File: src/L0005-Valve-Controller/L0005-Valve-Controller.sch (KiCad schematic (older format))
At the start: 25 parts, among them J1 Jumper_NO, J2 Jumper_NO, P1 3220-20-0200-00, P2 140-504-415-000, U1 LPC54113J256BD64QL, U2 LMS8117AMP-3.3_NOPB

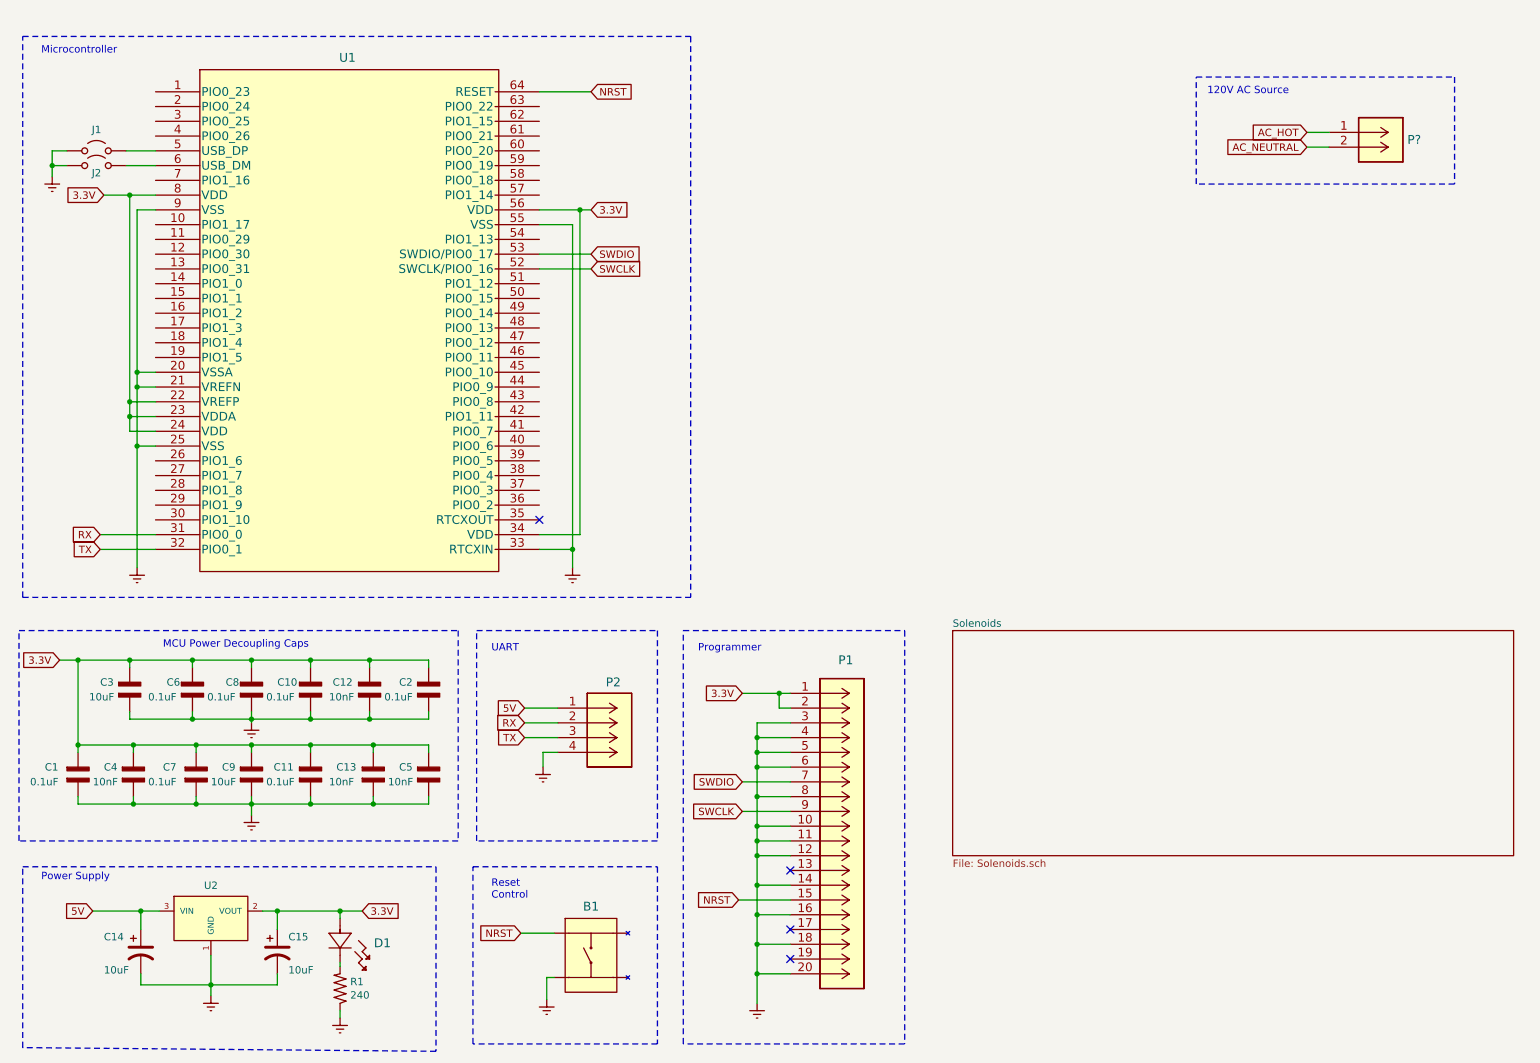
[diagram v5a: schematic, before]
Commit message: Added servo-actuated ball valves to schematic
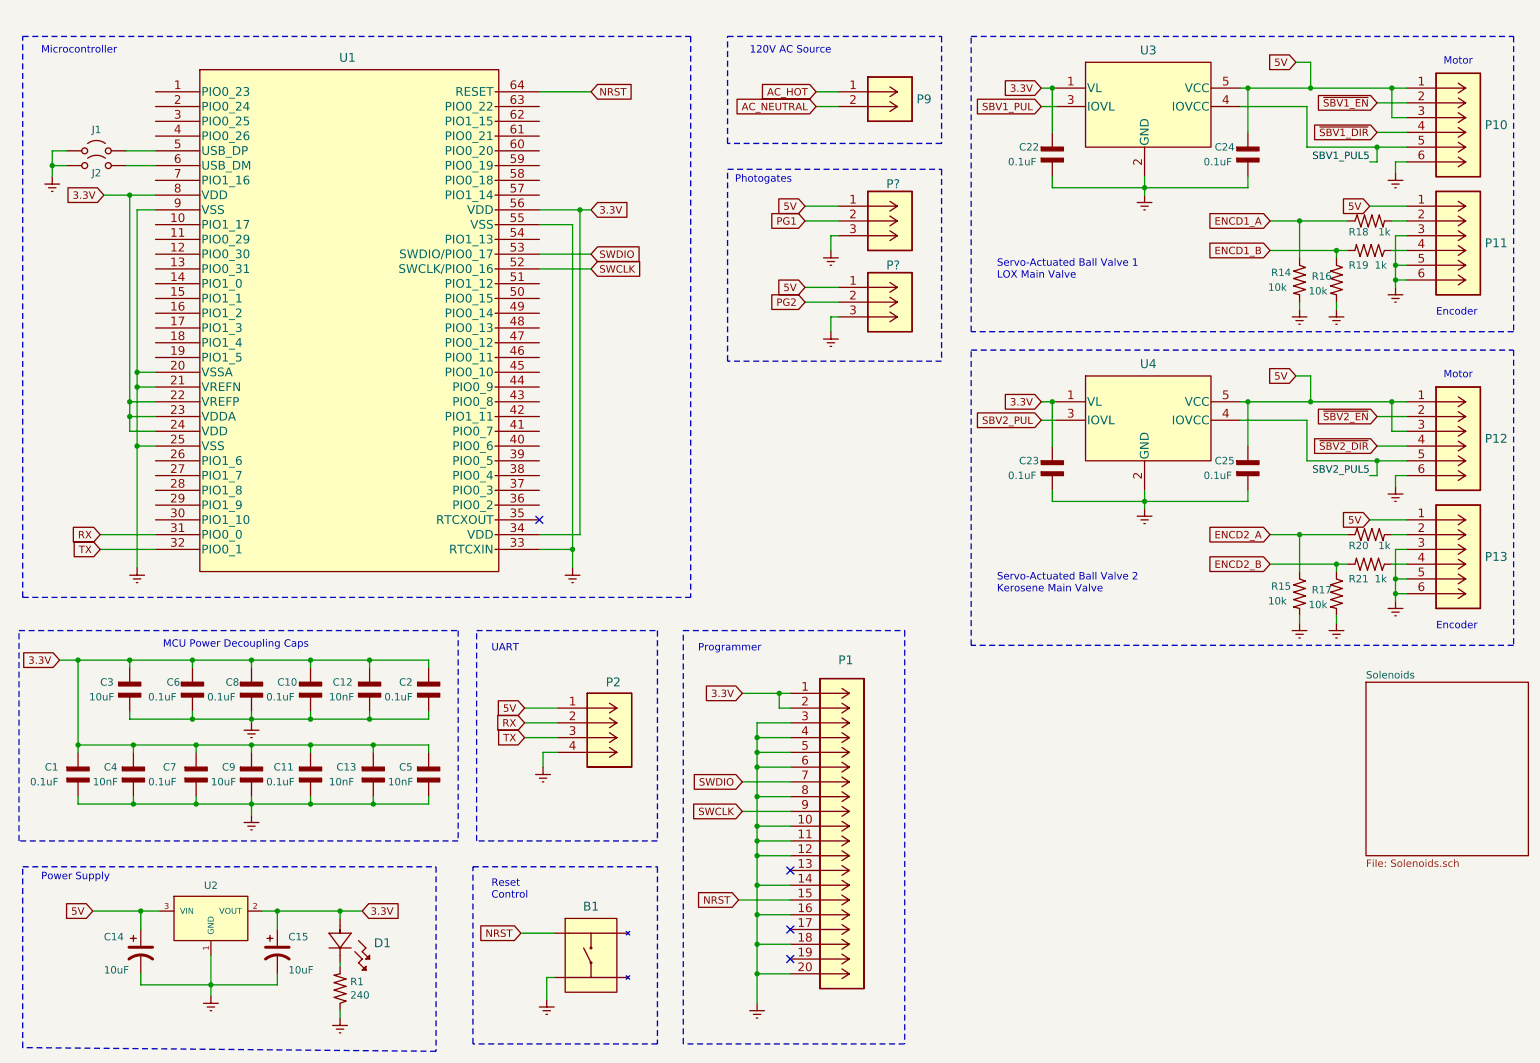
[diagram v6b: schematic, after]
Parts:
- added C22, C23, C24, C25: 0.1uF, symbol L0005-Valve-Controller:CAP_0603
- added P10, P11, P12, P13: 353620650, CONN_4840.2201_SCH, symbol L0005-Valve-Controller:353620650
- added P? (x2): 647676-3, CONN_2043-1X04G00DAU_OUP, symbol L0005-Valve-Controller:647676-3
- added R14, R15, R16, R17: 10k, symbol L0005-Valve-Controller:RES_0603
- added R18, R19, R20, R21: 1k, symbol L0005-Valve-Controller:RES_0603
- added U3, U4: MAX3370EXK+T, 21-0076E_MXM, symbol L0005-Valve-Controller:MAX3370EXK+T
- gave numbers to parts that had none: 1
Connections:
- net 3.3V: now also C22.2, C23.2, U3.1 (VL), U4.1 (VL)
- net 5V: now also C24.2, C25.2, P10.1 (+12V), P10.3, P11.1 (+12V), P12.1 (+12V), P12.3, P13.1 (+12V), P?.1, P?.1, U3.5 (VCC), U4.5 (VCC)
- net Earth: now also C22.1, C23.1, C24.1, C25.1, P10.6, P11.3, P11.5, P11.6, P12.6, P13.3, P13.5, P13.6, P?.3, P?.3, R14.2, R15.2, R16.2, R17.2, U3.2 (GND), U4.2 (GND)
- new net: P11.2 (GND), R18.2
- new net: P11.4, R19.1
- new net: P13.2 (GND), R20.2
- new net: P13.4, R21.1
- new net ENCD1_A: R14.1, R18.1
- new net ENCD1_B: R16.1, R19.2
- new net ENCD2_A: R15.1, R20.1
- new net ENCD2_B: R17.1, R21.2
- new net PG1: P?.2
- new net PG2: P?.2
- new net SBV1_PUL: U3.3 (IOVL)
- new net SBV1_PUL5: P10.5, U3.4 (IOVCC)
- new net SBV2_PUL: U4.3 (IOVL)
- new net SBV2_PUL5: P12.5, U4.4 (IOVCC)
- new net ~SBV1_DIR: P10.4
- new net ~SBV1_EN: P10.2 (GND)
- new net ~SBV2_DIR: P12.4
- new net ~SBV2_EN: P12.2 (GND)
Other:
- note added: "Encoder"
- note added: "Motor"
- note added: "Photogates"
- note added: "Servo-Actuated Ball Valve 1\nLOX Main Valve"
- note added: "Servo-Actuated Ball Valve 2\nKerosene Main Valve"
- moved on the sheet: P9
